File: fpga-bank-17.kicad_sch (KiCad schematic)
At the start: 1 part, among them U1 XC7K410T-2FFG900I

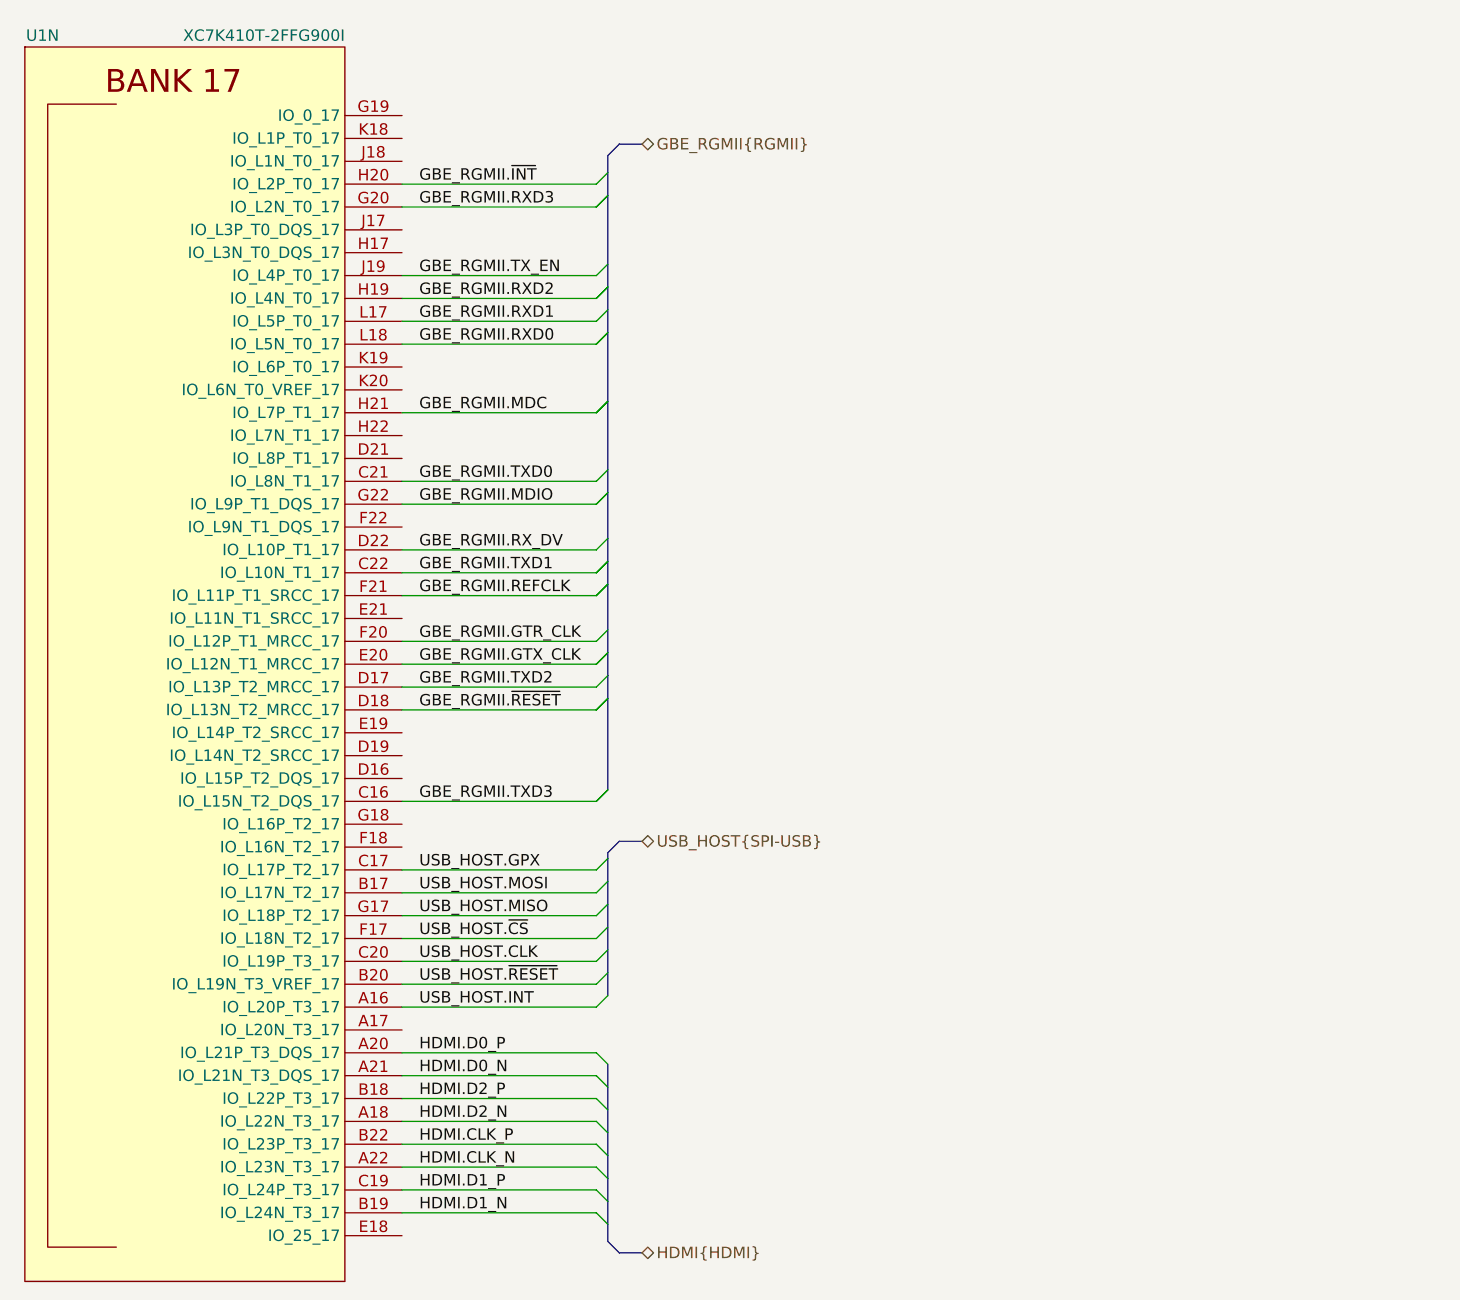
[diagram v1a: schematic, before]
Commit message: Improve placement of the GBE and USB Host PHY. Update pinout for better routing
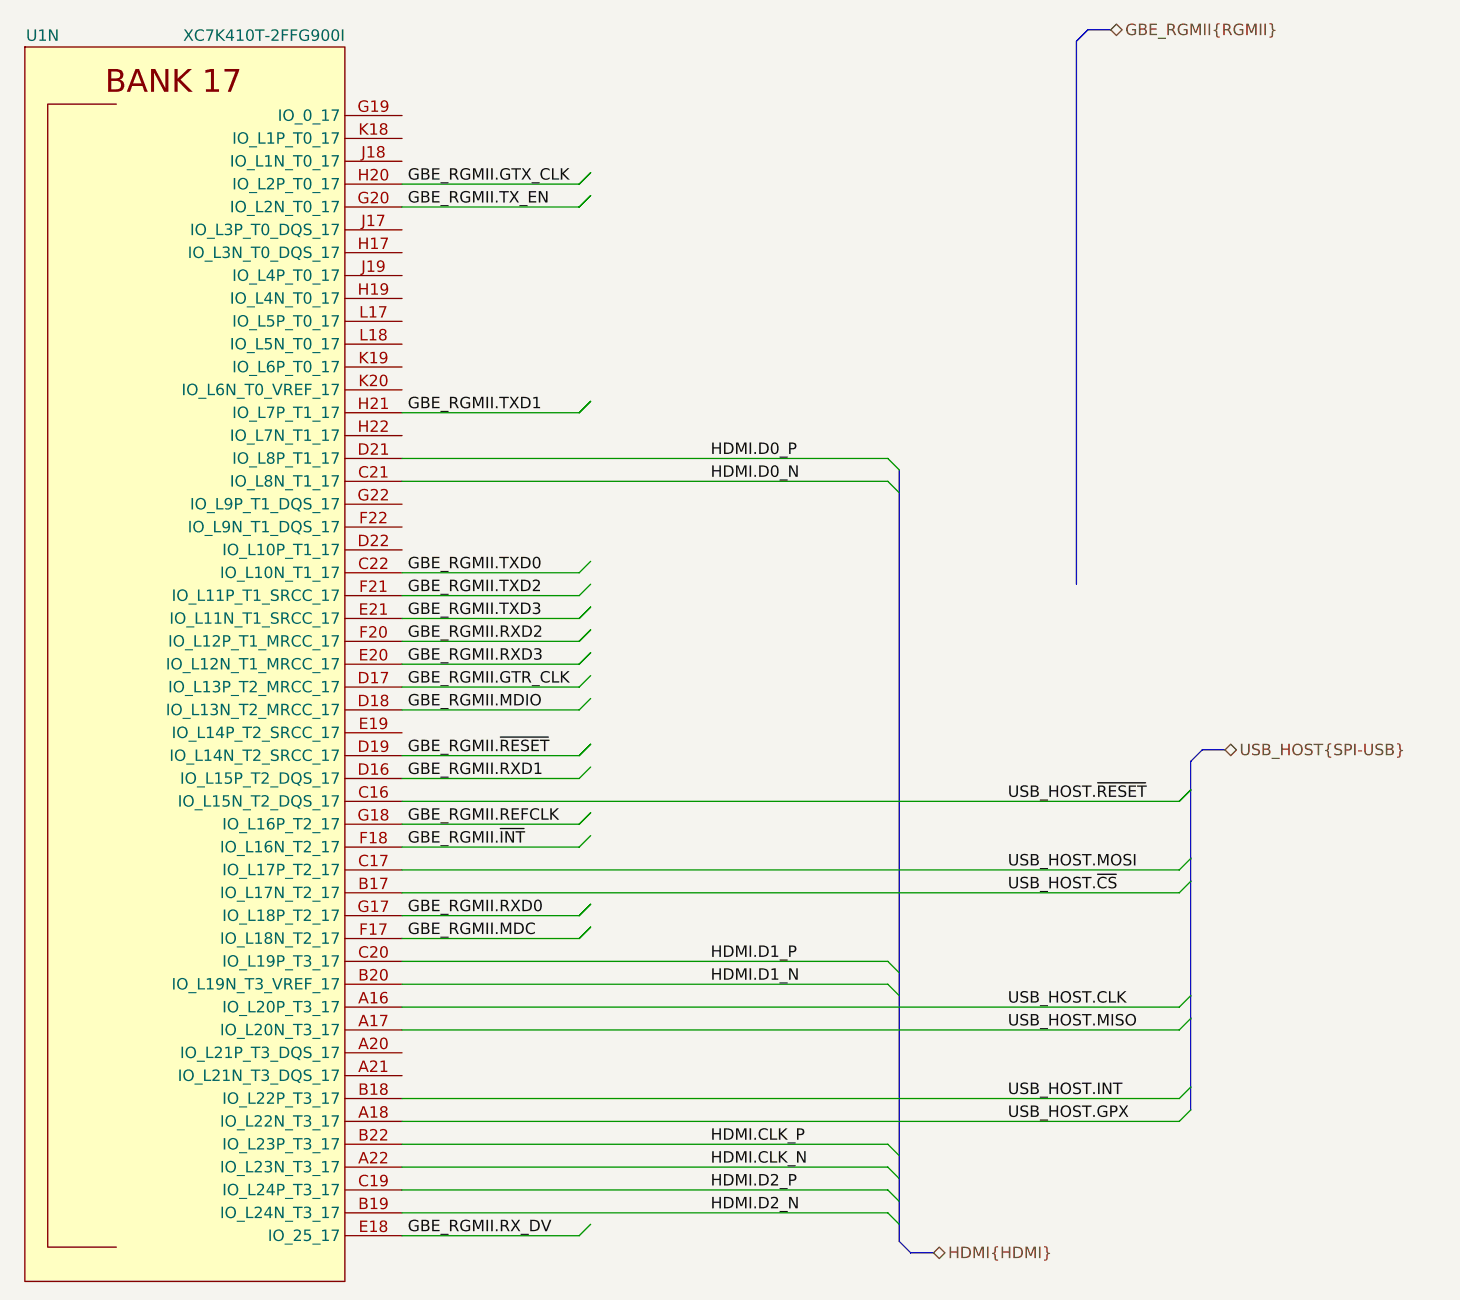
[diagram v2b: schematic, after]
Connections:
- net GBE_RGMII.GTR_CLK: now also U1.D17 (IO_L13P_T2_MRCC_17); no longer U1.F20 (IO_L12P_T1_MRCC_17)
- net GBE_RGMII.GTX_CLK: now also U1.H20 (IO_L2P_T0_17); no longer U1.E20 (IO_L12N_T1_MRCC_17)
- net GBE_RGMII.MDC: now also U1.F17 (IO_L18N_T2_17); no longer U1.H21 (IO_L7P_T1_17)
- net GBE_RGMII.MDIO: now also U1.D18 (IO_L13N_T2_MRCC_17); no longer U1.G22 (IO_L9P_T1_DQS_17)
- net GBE_RGMII.REFCLK: now also U1.G18 (IO_L16P_T2_17); no longer U1.F21 (IO_L11P_T1_SRCC_17)
- net GBE_RGMII.RXD0: now also U1.G17 (IO_L18P_T2_17); no longer U1.L18 (IO_L5N_T0_17)
- net GBE_RGMII.RXD1: now also U1.D16 (IO_L15P_T2_DQS_17); no longer U1.L17 (IO_L5P_T0_17)
- net GBE_RGMII.RXD2: now also U1.F20 (IO_L12P_T1_MRCC_17); no longer U1.H19 (IO_L4N_T0_17)
- net GBE_RGMII.RXD3: now also U1.E20 (IO_L12N_T1_MRCC_17); no longer U1.G20 (IO_L2N_T0_17)
- net GBE_RGMII.RX_DV: now also U1.E18 (IO_25_17); no longer U1.D22 (IO_L10P_T1_17)
- net GBE_RGMII.TXD0: now also U1.C22 (IO_L10N_T1_17); no longer U1.C21 (IO_L8N_T1_17)
- net GBE_RGMII.TXD1: now also U1.H21 (IO_L7P_T1_17); no longer U1.C22 (IO_L10N_T1_17)
- net GBE_RGMII.TXD2: now also U1.F21 (IO_L11P_T1_SRCC_17); no longer U1.D17 (IO_L13P_T2_MRCC_17)
- net GBE_RGMII.TXD3: now also U1.E21 (IO_L11N_T1_SRCC_17); no longer U1.C16 (IO_L15N_T2_DQS_17)
- net GBE_RGMII.TX_EN: now also U1.G20 (IO_L2N_T0_17); no longer U1.J19 (IO_L4P_T0_17)
- net GBE_RGMII.~{INT}: now also U1.F18 (IO_L16N_T2_17); no longer U1.H20 (IO_L2P_T0_17)
- net GBE_RGMII.~{RESET}: now also U1.D19 (IO_L14N_T2_SRCC_17); no longer U1.D18 (IO_L13N_T2_MRCC_17)
- net HDMI.D0_N: now also U1.C21 (IO_L8N_T1_17); no longer U1.A21 (IO_L21N_T3_DQS_17)
- net HDMI.D0_P: now also U1.D21 (IO_L8P_T1_17); no longer U1.A20 (IO_L21P_T3_DQS_17)
- net HDMI.D1_N: now also U1.B20 (IO_L19N_T3_VREF_17); no longer U1.B19 (IO_L24N_T3_17)
- net HDMI.D1_P: now also U1.C20 (IO_L19P_T3_17); no longer U1.C19 (IO_L24P_T3_17)
- net HDMI.D2_N: now also U1.B19 (IO_L24N_T3_17); no longer U1.A18 (IO_L22N_T3_17)
- net HDMI.D2_P: now also U1.C19 (IO_L24P_T3_17); no longer U1.B18 (IO_L22P_T3_17)
- net USB_HOST.CLK: now also U1.A16 (IO_L20P_T3_17); no longer U1.C20 (IO_L19P_T3_17)
- net USB_HOST.GPX: now also U1.A18 (IO_L22N_T3_17); no longer U1.C17 (IO_L17P_T2_17)
- net USB_HOST.INT: now also U1.B18 (IO_L22P_T3_17); no longer U1.A16 (IO_L20P_T3_17)
- net USB_HOST.MISO: now also U1.A17 (IO_L20N_T3_17); no longer U1.G17 (IO_L18P_T2_17)
- net USB_HOST.MOSI: now also U1.C17 (IO_L17P_T2_17); no longer U1.B17 (IO_L17N_T2_17)
- net USB_HOST.~{CS}: now also U1.B17 (IO_L17N_T2_17); no longer U1.F17 (IO_L18N_T2_17)
- net USB_HOST.~{RESET}: now also U1.C16 (IO_L15N_T2_DQS_17); no longer U1.B20 (IO_L19N_T3_VREF_17)

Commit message: Loclib
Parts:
- U1: footprint antmicro-footprints:xc7k410t-2ffg900I -> K410T-devboard-footprints:xc7k410t-2ffg900I; symbol antmicroMicrocontrollers:XC7K410T-2FFG900I -> K410T-devboard:XC7K410T-2FFG900I
